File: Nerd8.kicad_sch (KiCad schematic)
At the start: 3 parts, among them J10 Connector 02x01

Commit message: Kicad9
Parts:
- J10: footprint myfootprints:CONN2_1102030_OST -> Connector_AMASS:AMASS_XT60PW-M_1x02_P7.20mm_Horizontal; Distributor D -> (none); OrderNr ED2953-ND -> (none)
- renumbered D3 to D1
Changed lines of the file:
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@@
 (kicad_sch
-	(version 20231120)
+	(version 20250114)
 	(generator "eeschema")
-	(generator_version "8.0")
+	(generator_version "9.0")
 	(paper "A")
 	(title_block
@@
 		(on_board yes)
 		(dnp no)
-		(property "Reference" "#PWR012"
+		(property "Reference" "#PWR04"
 			(at 55.245 73.025 0)
 			(effects
@@
 		(on_board yes)
 		(dnp no)
-		(property "Reference" "D3"
+		(property "Reference" "D1"
 			(at 50.165 62.23 0)
 			(effects
@@
 			)
 		)
-		(property "Footprint" "myfootprints:CONN2_1102030_OST"
+		(property "Footprint" "Connector_AMASS:AMASS_XT60PW-M_1x02_P7.20mm_Horizontal"
 			(at 25.146 59.69 0)
 			(effects
@@
 			)
 		)
-		(property "Description" ""
+		(property "Description" "Amass XT60PW-M"
 			(at 33.782 54.61 0)
 			(effects
@@
 			)
 		)
-		(property "Distributor" "D"
+		(property "Distributor" ""
 			(at 33.782 54.61 0)
 			(effects
@@
 			)
 		)
-		(property "OrderNr" "ED2953-ND"
+		(property "OrderNr" ""
 			(at 33.782 54.61 0)
 			(effects
@@
 		(at 82.55 91.44)
 		(size 17.78 26.67)
+		(exclude_from_sim no)
+		(in_bom yes)
+		(on_board yes)
+		(dnp no)
 		(fields_autoplaced yes)
 		(stroke
@@
 		(at 82.55 46.355)
 		(size 17.145 33.02)
+		(exclude_from_sim no)
+		(in_bom yes)
+		(on_board yes)
+		(dnp no)
 		(stroke
 			(width 0.1524)
@@
 		(at 144.78 83.82)
 		(size 39.37 29.845)
+		(exclude_from_sim no)
+		(in_bom yes)
+		(on_board yes)
+		(dnp no)
 		(fields_autoplaced yes)
 		(stroke
@@
 		)
 	)
+	(embedded_fonts no)
 )

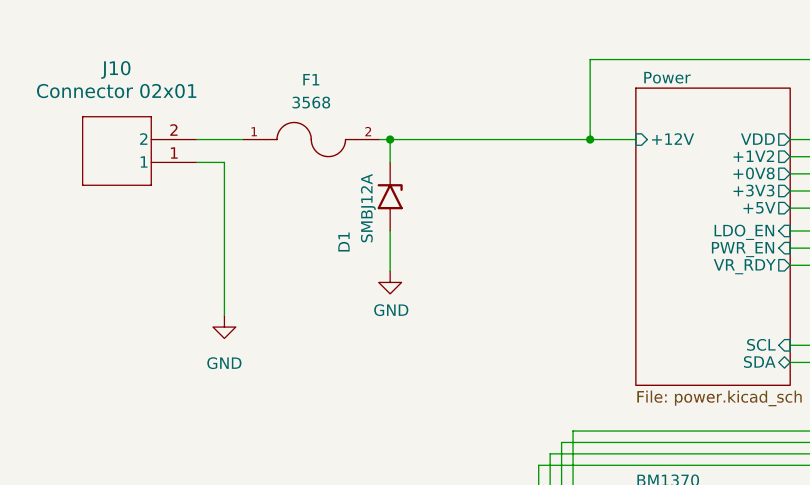
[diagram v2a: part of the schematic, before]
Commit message: board rev 3.0
- 6 phases using TPS53667
- Changed current MLCC capacitors to reduce BOM parts and rds on VRs
- Beads at LDOs, TDisplay, fans and Power input (EMC)
- Changed routing to allow better VDD circuit on bottom
- Reduced VDD area to avoid EMI
- New Layer distribution to reduce EMI
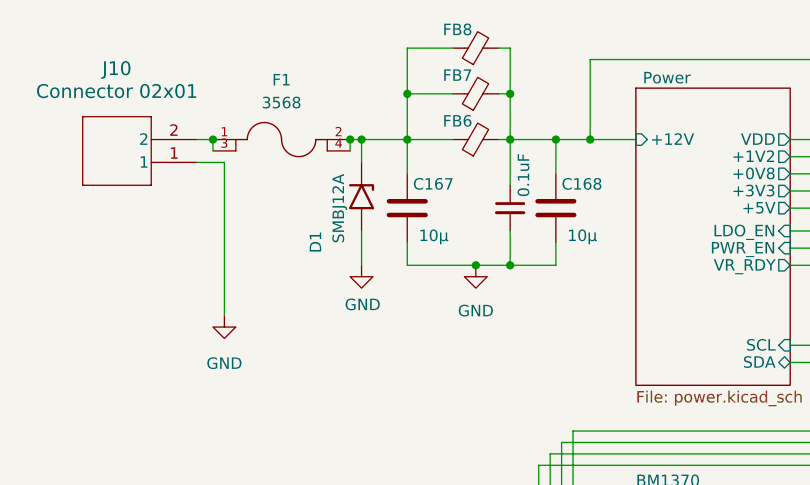
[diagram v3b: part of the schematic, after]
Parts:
- added C167, C168: 10µ, Capacitor_SMD:C_1210_3225Metric_Pad1.33x2.70mm_HandSolder, symbol Device:C
- added C170: 0.1uF, Capacitor_SMD:C_0603_1608Metric, symbol Device:C_Small
- added FB6, FB7, FB8: BLE32SN120SN1L, Resistor_SMD:R_1210_3225Metric_Pad1.30x2.65mm_HandSolder, symbol Device:FerriteBead_Small
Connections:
- net GND: now also C167.2, C168.2, C170.2
- net Power/+12V: now also C168.1, C170.1, FB6.2, FB7.2, FB8.2; no longer D1.1 (A1), F1.2
- net at F1.1, J10.2: now also F1.3
- new net: C167.1, D1.1 (A1), F1.2, F1.4, FB6.1, FB7.1, FB8.1
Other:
- moved on the sheet: D1

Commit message: Refactored buck stage and improved EMI performance
I've made several changes that I’d like to explain. Not sure yet if all of them are optimal, but they reflect my impressions and should help in several areas.

- Increased buck converter from 4 to 6 phases (now using TPS53667 controller).
- Changed layer stack to keep GND between VDD planes (to improve EMI).
- Added EMI filters at input, power beads, and additional ferrite beads in the 3V3 and 5V sections.
- Relocated the 5V LDO to optimize space in the regulator area.
- Standardized some input capacitors in the buck regulator stage.
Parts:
- C167, C168: LCSC (none) -> C89632
- C170: LCSC C92487 Hot -> C92487
- D1: LCSC (none) -> C113985
- F1: LCSC (none) -> C5249699
- FB6, FB7, FB8: LCSC (none) -> C5597997
- J10: LCSC (none) -> C98732
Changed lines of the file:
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@@
 			)
 		)
-		(property "LCSC" "C92487 Hot "
+		(property "LCSC" "C92487"
 			(at 68.58 59.69 0)
 			(effects
@@
 			)
 		)
+		(property "LCSC" "C5597997"
+			(at 64.77 46.99 90)
+			(effects
+				(font
+					(size 1.27 1.27)
+				)
+				(hide yes)
+			)
+		)
 		(pin "1"
 		)
@@
 			)
 		)
+		(property "LCSC" "C89632"
+			(at 57.15 59.69 0)
+			(effects
+				(font
+					(size 1.27 1.27)
+				)
+				(hide yes)
+			)
+		)
 		(pin "1"
 		)
@@
 		)
 		(property "OrderNr" "SMBJ12ALFCT-ND"
+			(at 52.07 58.42 0)
+			(effects
+				(font
+					(size 1.27 1.27)
+				)
+				(hide yes)
+			)
+		)
+		(property "LCSC" "C113985"
 			(at 52.07 58.42 0)
 			(effects
@@
 			)
 		)
+		(property "LCSC" "C5597997"
+			(at 64.77 41.91 90)
+			(effects
+				(font
+					(size 1.27 1.27)
+				)
+				(hide yes)
+			)
+		)
 		(pin "1"
 		)
@@
 			)
 		)
+		(property "LCSC" "C89632"
+			(at 73.66 59.69 0)
+			(effects
+				(font
+					(size 1.27 1.27)
+				)
+				(hide yes)
+			)
+		)
 		(pin "1"
 		)
@@
 			)
 		)
+		(property "LCSC" "C98732"
+			(at 33.782 54.61 0)
+			(effects
+				(font
+					(size 1.27 1.27)
+				)
+				(hide yes)
+			)
+		)
 		(pin "1"
 		)
@@
 			)
 		)
+		(property "LCSC" "C5249699"
+			(at 43.18 52.07 0)
+			(effects
+				(font
+					(size 1.27 1.27)
+				)
+				(hide yes)
+			)
+		)
 		(pin "1"
 		)
@@
 			(effects
 				(font
+					(size 1.27 1.27)
+				)
+				(hide yes)
+			)
+		)
+		(property "LCSC" "C5597997"
+			(at 64.77 52.07 90)
+			(effects
+				(font

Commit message: PCB w Tempmeasurement
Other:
- sheet BM1370 ports: added SCL, SDA, TEMP_A0, TEMP_A1; removed none
- sheet T-Display-S3 ports: added TEMP_A0, TEMP_A1; removed none
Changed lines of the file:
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@@
+	)
+	(junction
+		(at 125.73 105.664)
+		(diameter 0)
+		(color 0 0 0 0)
 	)
 	(junction
@@
 	)
 	(junction
+		(at 144.78 110.236)
+		(diameter 0)
+		(color 0 0 0 0)
+	)
+	(junction
 		(at 68.58 46.99)
 		(diameter 0)
@@
 	)
 	(junction
+		(at 124.46 107.95)
+		(diameter 0)
+		(color 0 0 0 0)
+	)
+	(junction
 		(at 35.56 52.07)
 		(diameter 0)
@@
 	(wire
 		(pts
+			(xy 144.78 110.236) (xy 145.034 110.236)
+		)
+		(stroke
+			(width 0)
+			(type default)
+		)
+	)
+	(wire
+		(pts
 			(xy 99.695 62.23) (xy 130.81 62.23)
 		)
@@
 	(wire
 		(pts
+			(xy 125.73 74.93) (xy 125.73 105.664)
+		)
+		(stroke
+			(width 0)
+			(type default)
+		)
+	)
+	(wire
+		(pts
 			(xy 57.15 63.5) (xy 57.15 66.04)
 		)
@@
 	(wire
 		(pts
-			(xy 125.73 74.93) (xy 125.73 106.045)
-		)
-		(stroke
-			(width 0)
-			(type default)
-		)
-	)
-	(wire
-		(pts
 			(xy 99.695 76.835) (xy 124.46 76.835)
 		)
@@
 	(wire
 		(pts
+			(xy 100.33 110.236) (xy 144.78 110.236)
+		)
+		(stroke
+			(width 0)
+			(type default)
+		)
+	)
+	(wire
+		(pts
 			(xy 74.295 99.695) (xy 82.55 99.695)
 		)
@@
 	(wire
 		(pts
+			(xy 100.33 105.664) (xy 125.73 105.664)
+		)
+		(stroke
+			(width 0)
+			(type default)
+		)
+	)
+	(wire
+		(pts
 			(xy 113.03 86.995) (xy 73.025 86.995)
 		)
@@
 	(wire
 		(pts
-			(xy 125.73 106.045) (xy 144.78 106.045)
+			(xy 124.46 107.95) (xy 144.78 107.95)
+		)
+		(stroke
+			(width 0)
+			(type default)
+		)
+	)
+	(wire
+		(pts
+			(xy 125.73 105.664) (xy 144.78 105.664)
 		)
 		(stroke
@@
 	(wire
 		(pts
+			(xy 100.33 107.95) (xy 124.46 107.95)
+		)
+		(stroke
+			(width 0)
+			(type default)
+		)
+	)
+	(wire
+		(pts
 			(xy 33.782 54.61) (xy 36.83 54.61)
 		)
@@
 	(wire
 		(pts
-			(xy 124.46 107.95) (xy 144.78 107.95)
-		)
-		(stroke
-			(width 0)
-			(type default)
-		)
-	)
-	(wire
-		(pts
 			(xy 77.47 52.07) (xy 82.55 52.07)
 		)
@@
 		(pts
 			(xy 130.81 62.23) (xy 130.81 92.71)
+		)
+		(stroke
+			(width 0)
+			(type default)
+		)
+	)
+	(wire
+		(pts
+			(xy 100.33 112.268) (xy 144.78 112.268)
 		)
 		(stroke
@@
 			)
 		)
+		(pin "SCL" input
+			(at 100.33 105.664 0)
+			(effects
+				(font
+					(size 1.27 1.27)
+				)
+				(justify right)
+			)
+		)
+		(pin "SDA" bidirectional
+			(at 100.33 107.95 0)
+			(effects
+				(font
+					(size 1.27 1.27)
+				)
+				(justify right)
+			)
+		)
+		(pin "TEMP_A0" input
+			(at 100.33 110.236 0)
+			(effects
+				(font
+					(size 1.27 1.27)
+				)
+				(justify right)
+			)
+		)
+		(pin "TEMP_A1" input
+			(at 100.33 112.268 0)
+			(effects
+				(font
+					(size 1.27 1.27)
+				)
+				(justify right)
+			)
+		)
 		(instances
 			(project "Nerd8"
@@
 		)
 		(pin "SCL" output
-			(at 144.78 106.045 180)
+			(at 144.78 105.664 180)
 			(effects
 				(font
@@
 			(effects
 				(font
+					(size 1.27 1.27)
+				)
+				(justify left)
+			)
+		)
+		(pin "TEMP_A0" input
+			(at 144.78 110.236 180)
+			(effects
+				(font
+					(size 1.27 1.27)
+				)
+				(justify left)
+			)
+		)
+		(pin "TEMP_A1" input
+			(at 144.78 112.268 180)
+			(effects
+				(font

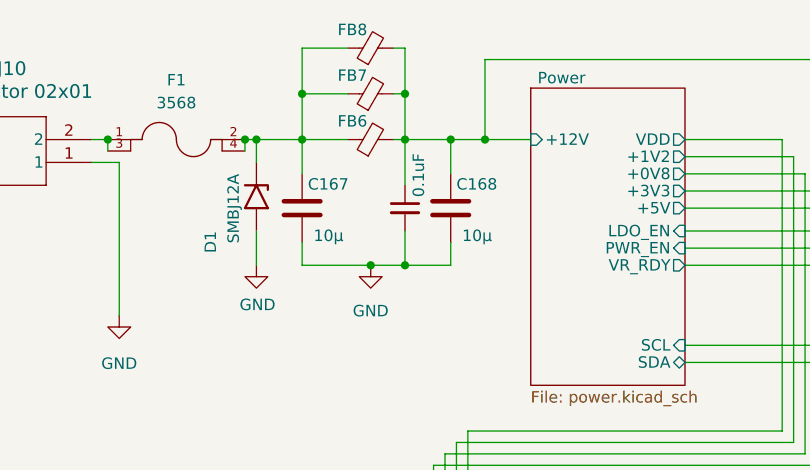
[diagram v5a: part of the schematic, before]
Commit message: Corrected Partnumbers (DK)
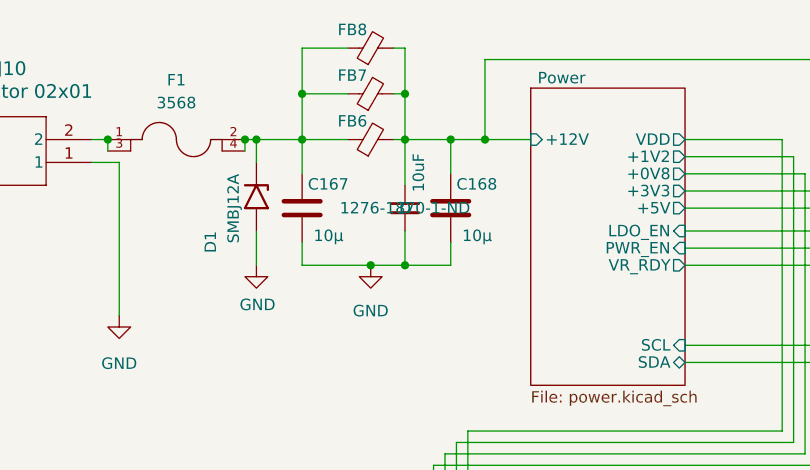
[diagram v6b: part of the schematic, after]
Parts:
- C170: value 0.1uF -> 10uF; Distributor (none) -> D; OrderNr (none) -> 1276-1870-1-ND
- FB6, FB7, FB8: Distributor (none) -> D; Manufacturer (none) -> BLE32SN120SN1L; OrderNr (none) -> 490-BLE32SN120SN1LCT-ND
- J10: Distributor (none) -> X
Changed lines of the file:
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@@
 			)
 		)
-		(property "Value" "0.1uF"
+		(property "Value" "10uF"
 			(at 70.104 53.594 90)
 			(effects
@@
 				)
 				(hide yes)
+			)
+		)
+		(property "Distributor" "D"
+			(at 68.58 59.69 0)
+			(effects
+				(font
+					(size 1.27 1.27)
+				)
+			)
+		)
+		(property "OrderNr" "1276-1870-1-ND"
+			(at 68.58 59.69 0)
+			(effects
+				(font
+					(size 1.27 1.27)
+				)
 			)
 		)
@@
 		)
 		(property "LCSC" "C5597997"
+			(at 64.77 46.99 90)
+			(effects
+				(font
+					(size 1.27 1.27)
+				)
+				(hide yes)
+			)
+		)
+		(property "Distributor" "D"
+			(at 64.77 46.99 90)
+			(effects
+				(font
+					(size 1.27 1.27)
+				)
+				(hide yes)
+			)
+		)
+		(property "OrderNr" "490-BLE32SN120SN1LCT-ND"
+			(at 64.77 46.99 90)
+			(effects
+				(font
+					(size 1.27 1.27)
+				)
+				(hide yes)
+			)
+		)
+		(property "Manufacturer" "BLE32SN120SN1L"
 			(at 64.77 46.99 90)
 			(effects
@@
 			)
 		)
+		(property "Distributor" "D"
+			(at 64.77 41.91 90)
+			(effects
+				(font
+					(size 1.27 1.27)
+				)
+				(hide yes)
+			)
+		)
+		(property "OrderNr" "490-BLE32SN120SN1LCT-ND"
+			(at 64.77 41.91 90)
+			(effects
+				(font
+					(size 1.27 1.27)
+				)
+				(hide yes)
+			)
+		)
+		(property "Manufacturer" "BLE32SN120SN1L"
+			(at 64.77 41.91 90)
+			(effects
+				(font
+					(size 1.27 1.27)
+				)
+				(hide yes)
+			)
+		)
 		(pin "1"
 		)
@@
 			)
 		)
-		(property "Distributor" ""
+		(property "Distributor" "X"
 			(at 33.782 54.61 0)
 			(effects
@@
 			(at 64.77 52.07 90)
 			(effects
+				(font
+					(size 1.27 1.27)
+				)
+				(hide yes)
+			)
+		)
+		(property "Distributor" "D"
+			(at 64.77 52.07 90)
+			(effects
+				(font
+					(size 1.27 1.27)
+				)
+				(hide yes)
+			)
+		)
+		(property "OrderNr" "490-BLE32SN120SN1LCT-ND"
+			(at 64.77 52.07 90)
+			(effects
+				(font
+					(size 1.27 1.27)
+				)
+				(hide yes)
+			)
+		)
+		(property "Manufacturer" "BLE32SN120SN1L"
+			(at 64.77 52.07 90)
+			(effects

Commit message: Board Rev + Bom
Changes to R-C Values Snubber
BOM / iBOM / Partnumbers
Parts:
- C167, C168: OrderNr 445-5984-1-ND -> 1276-6767-1-ND
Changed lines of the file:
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@@
 			)
 		)
-		(property "OrderNr" "445-5984-1-ND"
+		(property "OrderNr" "1276-6767-1-ND"
 			(at 57.15 59.69 0)
 			(effects
@@
 			)
 		)
-		(property "OrderNr" "445-5984-1-ND"
-			(at 73.66 59.69 0)
-			(effects
+		(property "OrderNr" "1276-6767-1-ND"
+			(at 73.66 59.69 0)
+			(effects

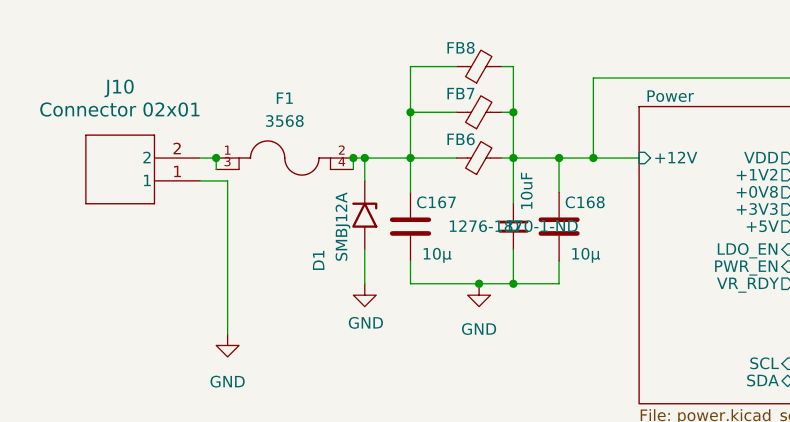
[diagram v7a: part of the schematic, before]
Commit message: Tmux Variant
- Added curcuit to read internal Asictemps per chip
- (i)BOM changes
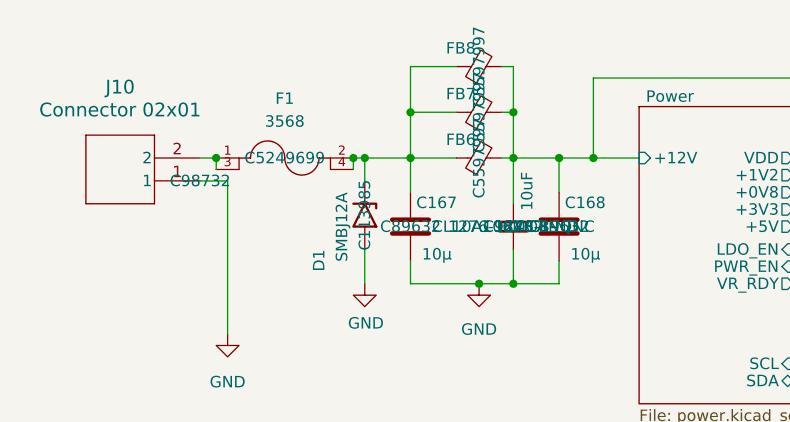
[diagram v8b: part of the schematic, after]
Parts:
- C167, C168: LCSC Part # (none) -> C89632
- C170: LCSC Part # (none) -> C92487; Manufacturer (none) -> CL10A106MO8NQNC
- D1: LCSC Part # (none) -> C113985
- F1: LCSC Part # (none) -> C5249699
- FB6, FB7, FB8: LCSC Part # (none) -> C5597997
- J10: LCSC Part # (none) -> C98732
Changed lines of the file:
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@@
+			)
+		)
+		(property "LCSC Part #" "C92487"
+			(at 68.58 59.69 0)
+			(effects
+				(font
+					(size 1.27 1.27)
+				)
+			)
+		)
+		(property "Manufacturer" "CL10A106MO8NQNC"
+			(at 68.58 59.69 0)
+			(effects
+				(font
+					(size 1.27 1.27)
+				)
 			)
 		)
@@
 				)
 				(hide yes)
+			)
+		)
+		(property "LCSC Part #" "C5597997"
+			(at 64.77 46.99 0)
+			(effects
+				(font
+					(size 1.27 1.27)
+				)
 			)
 		)
@@
 			)
 		)
+		(property "LCSC Part #" "C89632"
+			(at 57.15 59.69 0)
+			(effects
+				(font
+					(size 1.27 1.27)
+				)
+			)
+		)
 		(pin "1"
 		)
@@
 			)
 		)
+		(property "LCSC Part #" "C113985"
+			(at 52.07 58.42 0)
+			(effects
+				(font
+					(size 1.27 1.27)
+				)
+			)
+		)
 		(pin "1"
 		)
@@
 				)
 				(hide yes)
+			)
+		)
+		(property "LCSC Part #" "C5597997"
+			(at 64.77 41.91 0)
+			(effects
+				(font
+					(size 1.27 1.27)
+				)
 			)
 		)
@@
 			)
 		)
+		(property "LCSC Part #" "C89632"
+			(at 73.66 59.69 0)
+			(effects
+				(font
+					(size 1.27 1.27)
+				)
+			)
+		)
 		(pin "1"
 		)
@@
 			)
 		)
+		(property "LCSC Part #" "C98732"
+			(at 33.782 54.61 0)
+			(effects
+				(font
+					(size 1.27 1.27)
+				)
+			)
+		)
 		(pin "1"
 		)
@@
 			)
 		)
+		(property "LCSC Part #" "C5249699"
+			(at 43.18 52.07 0)
+			(effects
+				(font
+					(size 1.27 1.27)
+				)
+			)
+		)
 		(pin "1"
 		)
@@
 			)
 		)
+		(property "LCSC Part #" "C5597997"
+			(at 64.77 52.07 0)
+			(effects
+				(font
+					(size 1.27 1.27)
+				)
+			)
+		)
